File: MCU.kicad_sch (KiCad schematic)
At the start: 47 parts, among them J1 SWD_LOG, Q2 BC847, SW1 SW_Push, U1 STM32F429IGTx, Y1 25MHz, Y5 32.768KHz

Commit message: None.
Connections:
- net SWCLK: now also J1.2 (Pin_2); no longer J1.1 (Pin_1)
- net SWDIO: now also J1.4 (Pin_4); no longer J1.3 (Pin_3)
- net at R6.1: now also J1.3 (Pin_3); no longer J1.4 (Pin_4)
- net at R5.1: now also J1.1 (Pin_1); no longer J1.2 (Pin_2)
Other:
- moved on the sheet: C6, R5, R6
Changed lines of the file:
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@@
     )
   )
-  (global_label "SWCLK" (shape bidirectional) (at 220.98 200.66 180) (fields_autoplaced)
-    (effects (font (size 1.27 1.27)) (justify right))
-    (property "Intersheetrefs" "${INTERSHEET_REFS}" (at 212.3379 200.7394 0)
-      (effects (font (size 1.27 1.27)) (justify right) hide)
+  (global_label "SWCLK" (shape bidirectional) (at 233.68 200.66 0) (fields_autoplaced)
+    (effects (font (size 1.27 1.27)) (justify left))
+    (property "Intersheetrefs" "${INTERSHEET_REFS}" (at 242.3221 200.7394 0)
+      (effects (font (size 1.27 1.27)) (justify left) hide)
     )
   )
@@
     )
   )
-  (global_label "SWDIO" (shape bidirectional) (at 220.98 203.2 180) (fields_autoplaced)
-    (effects (font (size 1.27 1.27)) (justify right))
-    (property "Intersheetrefs" "${INTERSHEET_REFS}" (at 212.7007 203.2794 0)
-      (effects (font (size 1.27 1.27)) (justify right) hide)
+  (global_label "SWDIO" (shape bidirectional) (at 233.68 203.2 0) (fields_autoplaced)
+    (effects (font (size 1.27 1.27)) (justify left))
+    (property "Intersheetrefs" "${INTERSHEET_REFS}" (at 241.9593 203.2794 0)
+      (effects (font (size 1.27 1.27)) (justify left) hide)
     )
   )
@@
     )
   )
-  (global_label "USART6_RX" (shape bidirectional) (at 238.76 203.2 0) (fields_autoplaced)
-    (effects (font (size 1.27 1.27)) (justify left))
-    (property "Intersheetrefs" "${INTERSHEET_REFS}" (at 0 -2.54 0)
-      (effects (font (size 1.27 1.27)) hide)
-    )
-  )
-  (global_label "USART6_TX" (shape bidirectional) (at 238.76 200.66 0) (fields_autoplaced)
-    (effects (font (size 1.27 1.27)) (justify left))
-    (property "Intersheetrefs" "${INTERSHEET_REFS}" (at 0 -2.54 0)
+  (global_label "USART6_RX" (shape bidirectional) (at 215.9 203.2 180) (fields_autoplaced)
+    (effects (font (size 1.27 1.27)) (justify right))
+    (property "Intersheetrefs" "${INTERSHEET_REFS}" (at 454.66 -2.54 0)
+      (effects (font (size 1.27 1.27)) hide)
+    )
+  )
+  (global_label "USART6_TX" (shape bidirectional) (at 215.9 200.66 180) (fields_autoplaced)
+    (effects (font (size 1.27 1.27)) (justify right))
+    (property "Intersheetrefs" "${INTERSHEET_REFS}" (at 454.66 -2.54 0)
       (effects (font (size 1.27 1.27)) hide)
     )
@@
     )
   )
-  (symbol (lib_id "Device:C_Small") (at 205.74 203.2 180) (unit 1)
-    (in_bom yes) (on_board yes) (dnp no)
-    (property "Reference" "C6" (at 204.47 205.74 90)
-      (effects (font (size 1.27 1.27)))
-    )
-    (property "Value" "10uF" (at 204.47 198.12 90)
-      (effects (font (size 1.27 1.27)))
-    )
-    (property "Footprint" "Anh_Footprints:C_1206" (at 205.74 203.2 0)
-      (effects (font (size 1.27 1.27)) hide)
-    )
-    (property "Datasheet" "~" (at 205.74 203.2 0)
+  (symbol (lib_id "Device:C_Small") (at 196.85 201.93 180) (unit 1)
+    (in_bom yes) (on_board yes) (dnp no)
+    (property "Reference" "C6" (at 195.58 204.47 90)
+      (effects (font (size 1.27 1.27)))
+    )
+    (property "Value" "10uF" (at 195.58 196.85 90)
+      (effects (font (size 1.27 1.27)))
+    )
+    (property "Footprint" "Anh_Footprints:C_1206" (at 196.85 201.93 0)
+      (effects (font (size 1.27 1.27)) hide)
+    )
+    (property "Datasheet" "~" (at 196.85 201.93 0)
       (effects (font (size 1.27 1.27)) hide)
     )
@@
     )
   )
-  (symbol (lib_id "power:+3.3V") (at 205.74 200.66 0) (mirror y) (unit 1)
+  (symbol (lib_id "power:+3.3V") (at 196.85 199.39 0) (mirror y) (unit 1)
     (in_bom yes) (on_board yes) (dnp no) (fields_autoplaced)
-    (property "Reference" "#PWR017" (at 205.74 204.47 0)
-      (effects (font (size 1.27 1.27)) hide)
-    )
-    (property "Value" "+3.3V" (at 205.74 195.58 0)
-      (effects (font (size 1.27 1.27)))
-    )
-    (property "Footprint" "" (at 205.74 200.66 0)
-      (effects (font (size 1.27 1.27)) hide)
-    )
-    (property "Datasheet" "" (at 205.74 200.66 0)
+    (property "Reference" "#PWR017" (at 196.85 203.2 0)
+      (effects (font (size 1.27 1.27)) hide)
+    )
+    (property "Value" "+3.3V" (at 196.85 194.31 0)
+      (effects (font (size 1.27 1.27)))
+    )
+    (property "Footprint" "" (at 196.85 199.39 0)
+      (effects (font (size 1.27 1.27)) hide)
+    )
+    (property "Datasheet" "" (at 196.85 199.39 0)
       (effects (font (size 1.27 1.27)) hide)
     )
@@
     )
   )
-  (symbol (lib_id "Device:R_Small") (at 236.22 203.2 90) (unit 1)
-    (in_bom yes) (on_board yes) (dnp no)
-    (property "Reference" "R6" (at 232.41 204.47 90)
-      (effects (font (size 1.27 1.27)))
-    )
-    (property "Value" "100" (at 236.22 203.2 90)
-      (effects (font (size 1.27 1.27)))
-    )
-    (property "Footprint" "Anh_Footprints:R_0603" (at 236.22 203.2 0)
-      (effects (font (size 1.27 1.27)) hide)
-    )
-    (property "Datasheet" "~" (at 236.22 203.2 0)
+  (symbol (lib_id "Device:R_Small") (at 218.44 203.2 270) (mirror x) (unit 1)
+    (in_bom yes) (on_board yes) (dnp no)
+    (property "Reference" "R6" (at 222.25 204.47 90)
+      (effects (font (size 1.27 1.27)))
+    )
+    (property "Value" "100" (at 218.44 203.2 90)
+      (effects (font (size 1.27 1.27)))
+    )
+    (property "Footprint" "Anh_Footprints:R_0603" (at 218.44 203.2 0)
+      (effects (font (size 1.27 1.27)) hide)
+    )
+    (property "Datasheet" "~" (at 218.44 203.2 0)
       (effects (font (size 1.27 1.27)) hide)
     )
@@
     )
   )
-  (symbol (lib_id "Device:R_Small") (at 236.22 200.66 90) (unit 1)
-    (in_bom yes) (on_board yes) (dnp no)
-    (property "Reference" "R5" (at 232.41 201.93 90)
-      (effects (font (size 1.27 1.27)))
-    )
-    (property "Value" "100" (at 236.22 200.66 90)
-      (effects (font (size 1.27 1.27)))
-    )
-    (property "Footprint" "Anh_Footprints:R_0603" (at 236.22 200.66 0)
-      (effects (font (size 1.27 1.27)) hide)
-    )
-    (property "Datasheet" "~" (at 236.22 200.66 0)
+  (symbol (lib_id "Device:R_Small") (at 218.44 200.66 270) (mirror x) (unit 1)
+    (in_bom yes) (on_board yes) (dnp no)
+    (property "Reference" "R5" (at 222.25 201.93 90)
+      (effects (font (size 1.27 1.27)))
+    )
+    (property "Value" "100" (at 218.44 200.66 90)
+      (effects (font (size 1.27 1.27)))
+    )
+    (property "Footprint" "Anh_Footprints:R_0603" (at 218.44 200.66 0)
+      (effects (font (size 1.27 1.27)) hide)
+    )
+    (property "Datasheet" "~" (at 218.44 200.66 0)
       (effects (font (size 1.27 1.27)) hide)
     )
@@
     )
   )
-  (symbol (lib_id "power:GND") (at 205.74 205.74 0) (mirror y) (unit 1)
+  (symbol (lib_id "power:GND") (at 196.85 204.47 0) (mirror y) (unit 1)
     (in_bom yes) (on_board yes) (dnp no) (fields_autoplaced)
-    (property "Reference" "#PWR018" (at 205.74 212.09 0)
-      (effects (font (size 1.27 1.27)) hide)
-    )
-    (property "Value" "GND" (at 205.74 210.82 0)
-      (effects (font (size 1.27 1.27)))
-    )
-    (property "Footprint" "" (at 205.74 205.74 0)
-      (effects (font (size 1.27 1.27)) hide)
-    )
-    (property "Datasheet" "" (at 205.74 205.74 0)
-      (effects (font (size 1.27 1.27)) hide)
-    )
+    (property "Reference" "#PWR018" (at 196.85 210.82 0)
+      (effects (font (size 1.27 1.27)) hide)
+    )
+    (property "Value" "GND" (at 196.85 209.55 0)
+      (effects (font (size 1.27 1.27)))
+    )
+    (property "Footprint" "" (at 196.85 204.47 0)
+      (effects (font (size 1.27 1.27)) hide)
+    )
+    (property "Datasheet" "" (at 196.85 204.47 0)
+      (effects (font (size 1.27 1.27)) hide)
+    )

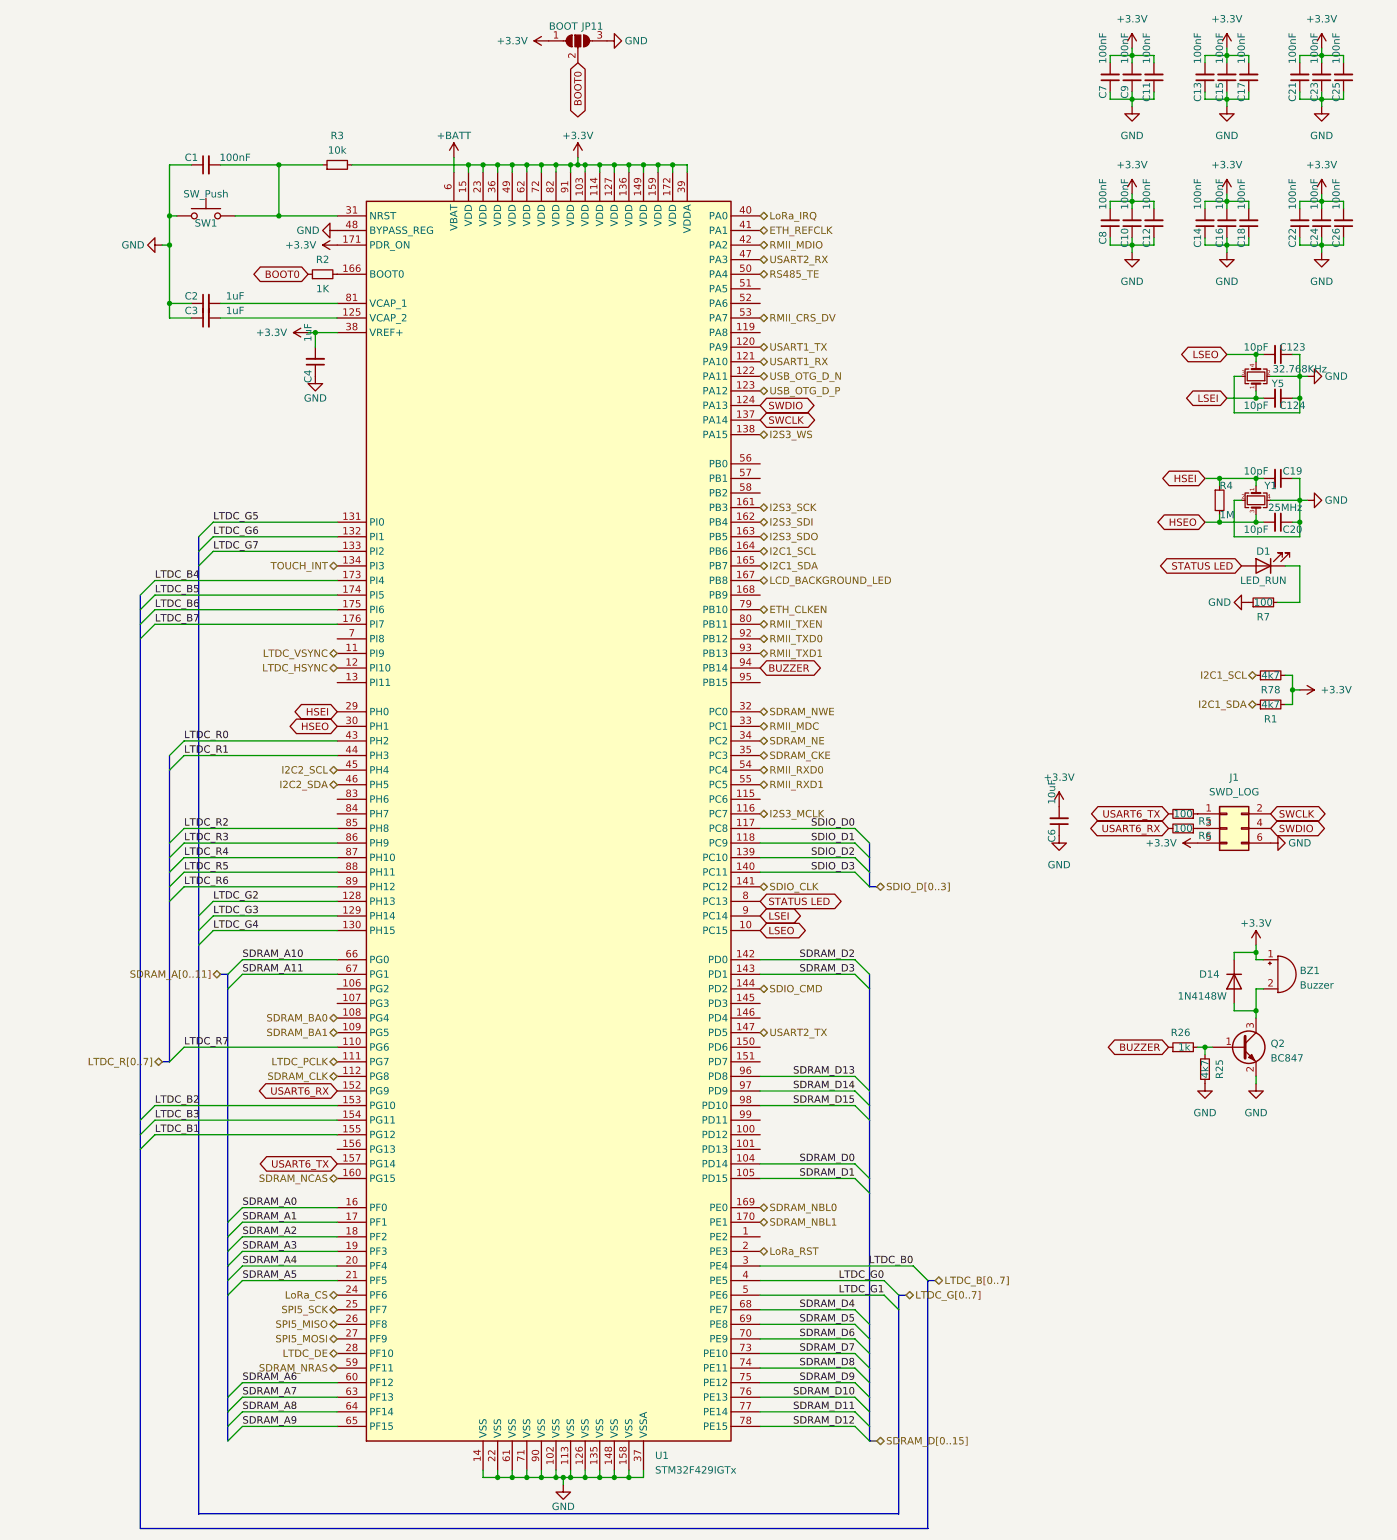
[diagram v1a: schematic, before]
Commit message: Fix USB silkscreen name.
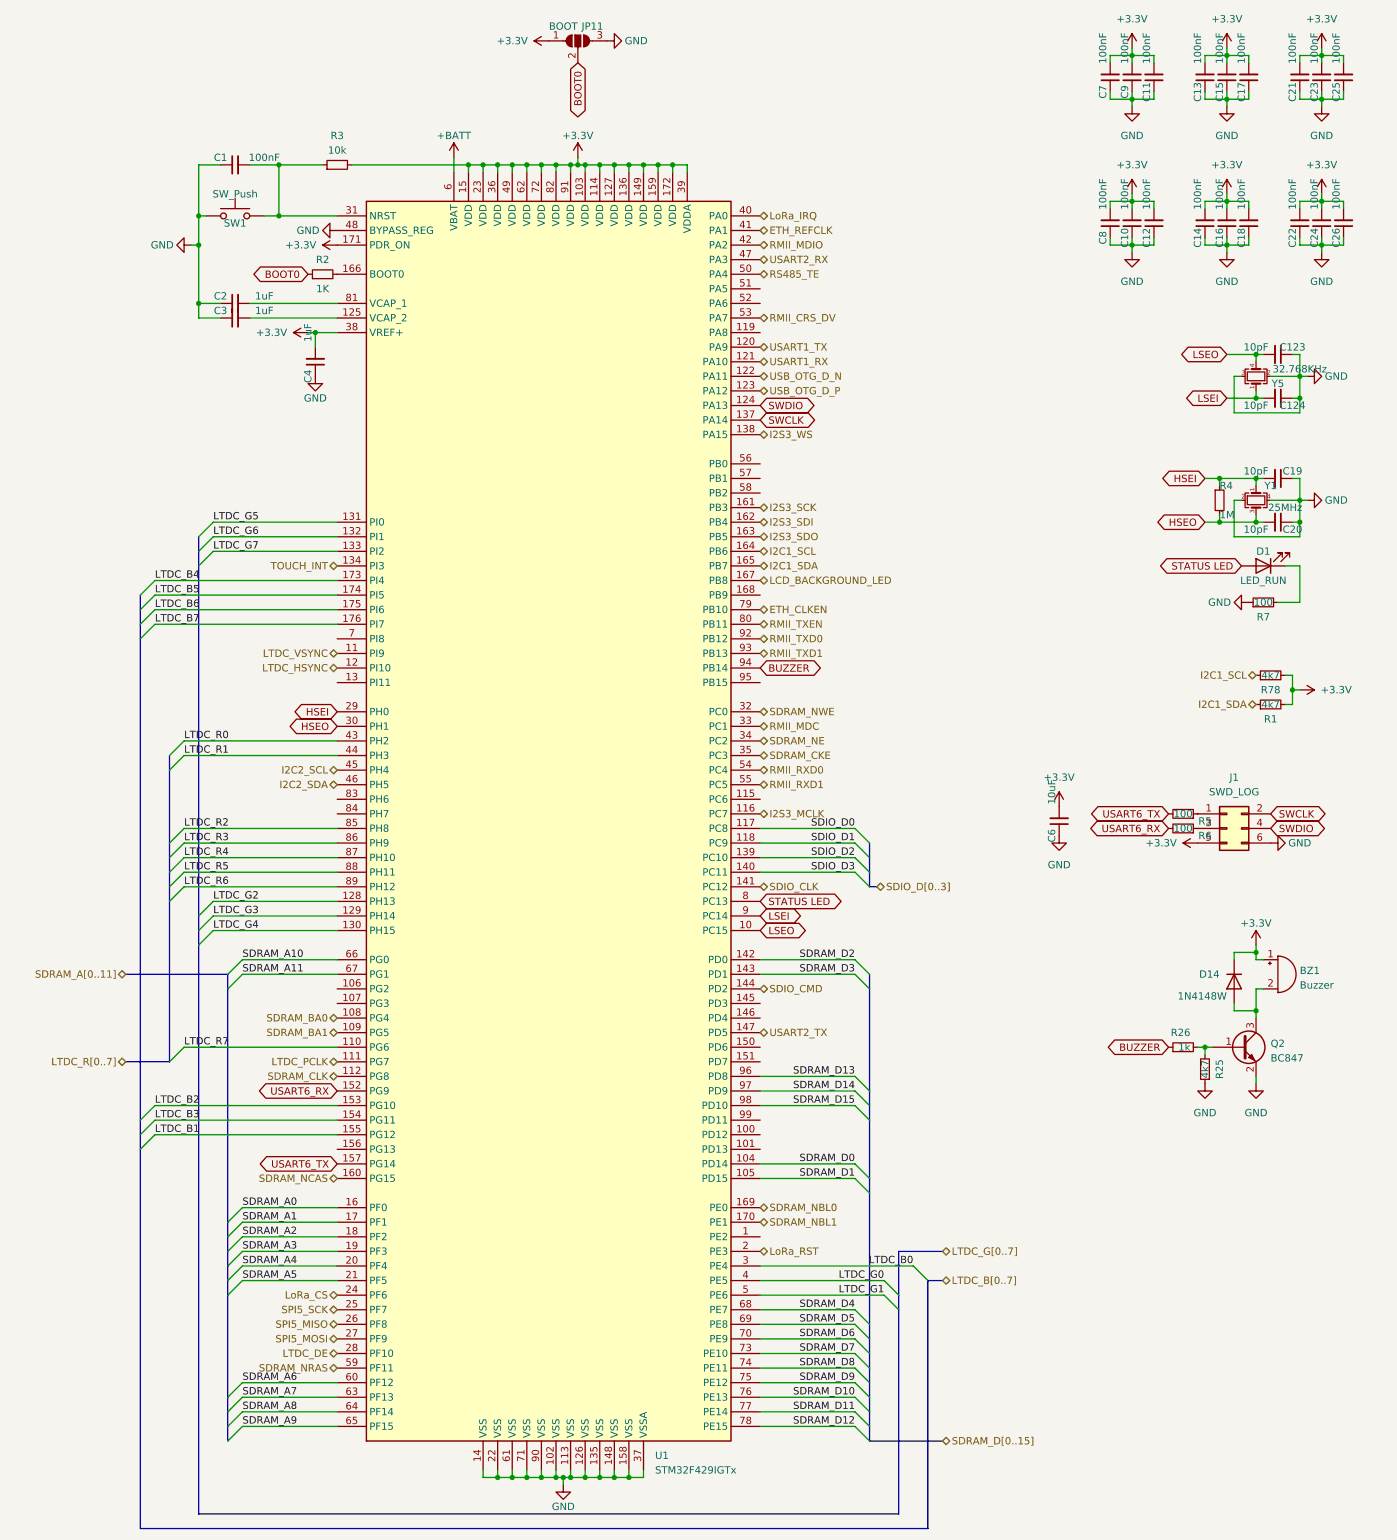
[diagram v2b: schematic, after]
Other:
- moved on the sheet: C1, C2, C3, SW1
